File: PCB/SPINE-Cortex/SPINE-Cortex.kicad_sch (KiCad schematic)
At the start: 78 parts, among them J1 SWD, J2 Conn_01x08, J3 Conn_01x02, J4 CAN_IN, J5 CAN_OUT, U1 STM32F103C8Tx, U4 MIC5219-3.3YM5, U5 TCAN1044V, U7 TPS54240DGQ, Y1 Resonator

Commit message: Finish Vertebra
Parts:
- removed C6: 100nF, Capacitor_SMD:C_0603_1608Metric, symbol Device:C_Small
- removed J2: Conn_01x08, Connector_JST:JST_GH_SM08B-GHS-TB_1x08-1MP_P1.25mm_Horizontal, symbol Connector_Generic:Conn_01x08
- removed J3: Conn_01x02, Connector_PinHeader_2.00mm:PinHeader_1x02_P2.00mm_Vertical, symbol Connector_Generic:Conn_01x02
- removed R17: 10K, Resistor_SMD:R_0603_1608Metric, symbol Device:R_Small
- removed U1: STM32F103C8Tx, Package_QFP:LQFP-48_7x7mm_P0.5mm, symbol MCU_ST_STM32F1:STM32F103C8Tx
- added C1: 100nF, Capacitor_SMD:C_0603_1608Metric, symbol Device:C
- added J2: Conn_01x06, Connector_JST:JST_GH_SM06B-GHS-TB_1x06-1MP_P1.25mm_Horizontal, symbol Connector_Generic:Conn_01x06
- added R16: 120R, Resistor_SMD:R_0603_1608Metric, symbol Device:R_Small
- added U1: STM32G431RBTx, Package_QFP:LQFP-64_10x10mm_P0.5mm, symbol MCU_ST_STM32G4:STM32G431RBTx
- added U3: SP3485EN, Package_SO:SOIC-8_3.9x4.9mm_P1.27mm, symbol Interface_UART:SP3485EN
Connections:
- net +3.3V: now also U1.1 (VBAT), U1.16 (VDD), U1.32 (VDD), U1.48 (VDD), U1.64 (VDD)
- net +5V: now also C1.2, J2.2 (Pin_2), U3.8 (VCC)
- net BOOT: now also U1.7 (PG10)
- net CANRX: now also U1.45 (PA11)
- net CANTX: now also U1.46 (PA12)
- net GND: now also C1.1, J2.1 (Pin_1), U1.15 (VSS), U1.27 (VSSA), U1.31 (VSS), U1.47 (VSS), U1.63 (VSS), U3.5 (GND)
- net Reset: now also U1.28 (VREF+)
- net SWCLK: now also U1.50 (PA14)
- net SWDIO: now also U1.49 (PA13)
- net VREF: now also U1.29 (VDDA)
- net at Y1.1: now also U1.5 (PF0)
- net at Y1.3: now also U1.6 (PF1)
- new net ENABLE: J2.6 (Pin_6)
- new net FAULT: J2.5 (Pin_5)
- new net RS485_A: J2.3 (Pin_3), R16.1, U3.6 (A)
- new net RS485_B: J2.4 (Pin_4), R16.2, U3.7 (B)
- new net USART2_DE: U3.2 (~{RE}), U3.3 (DE)
- new net USART2_RX: U3.1 (RO)
- new net USART2_TX: U3.4 (DI)
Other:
- moved on the sheet: C21, C23, C24, C26, C28, C31, C4, FB1, H5, H6, J1, J4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

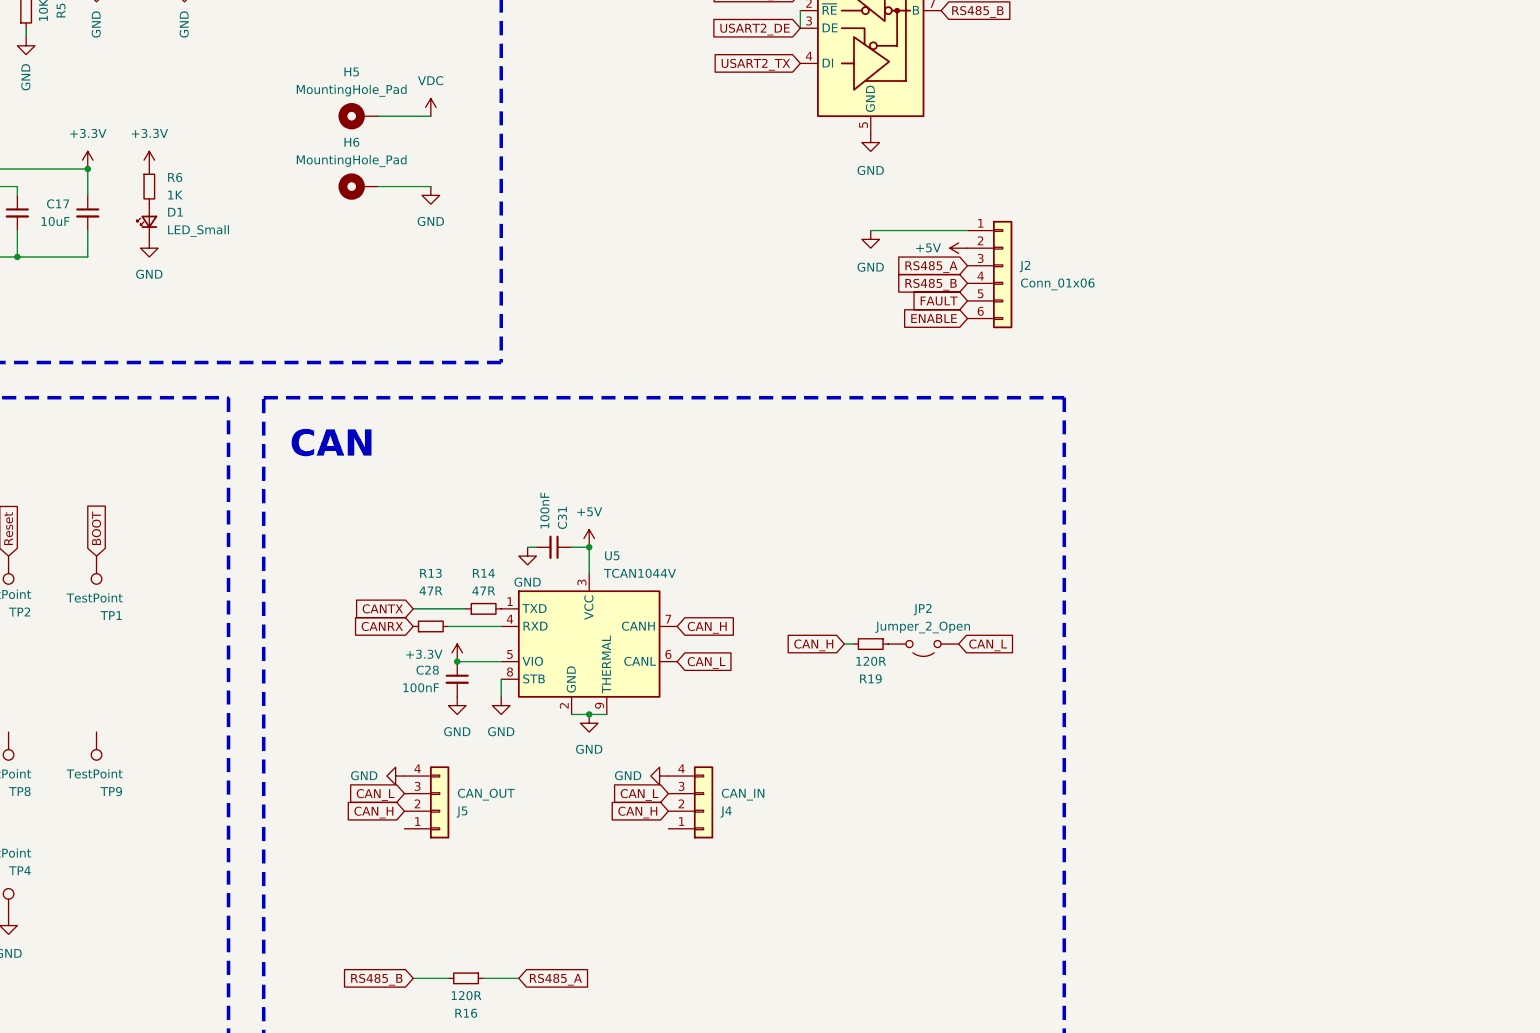
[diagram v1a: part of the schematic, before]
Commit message: Vertebra fix
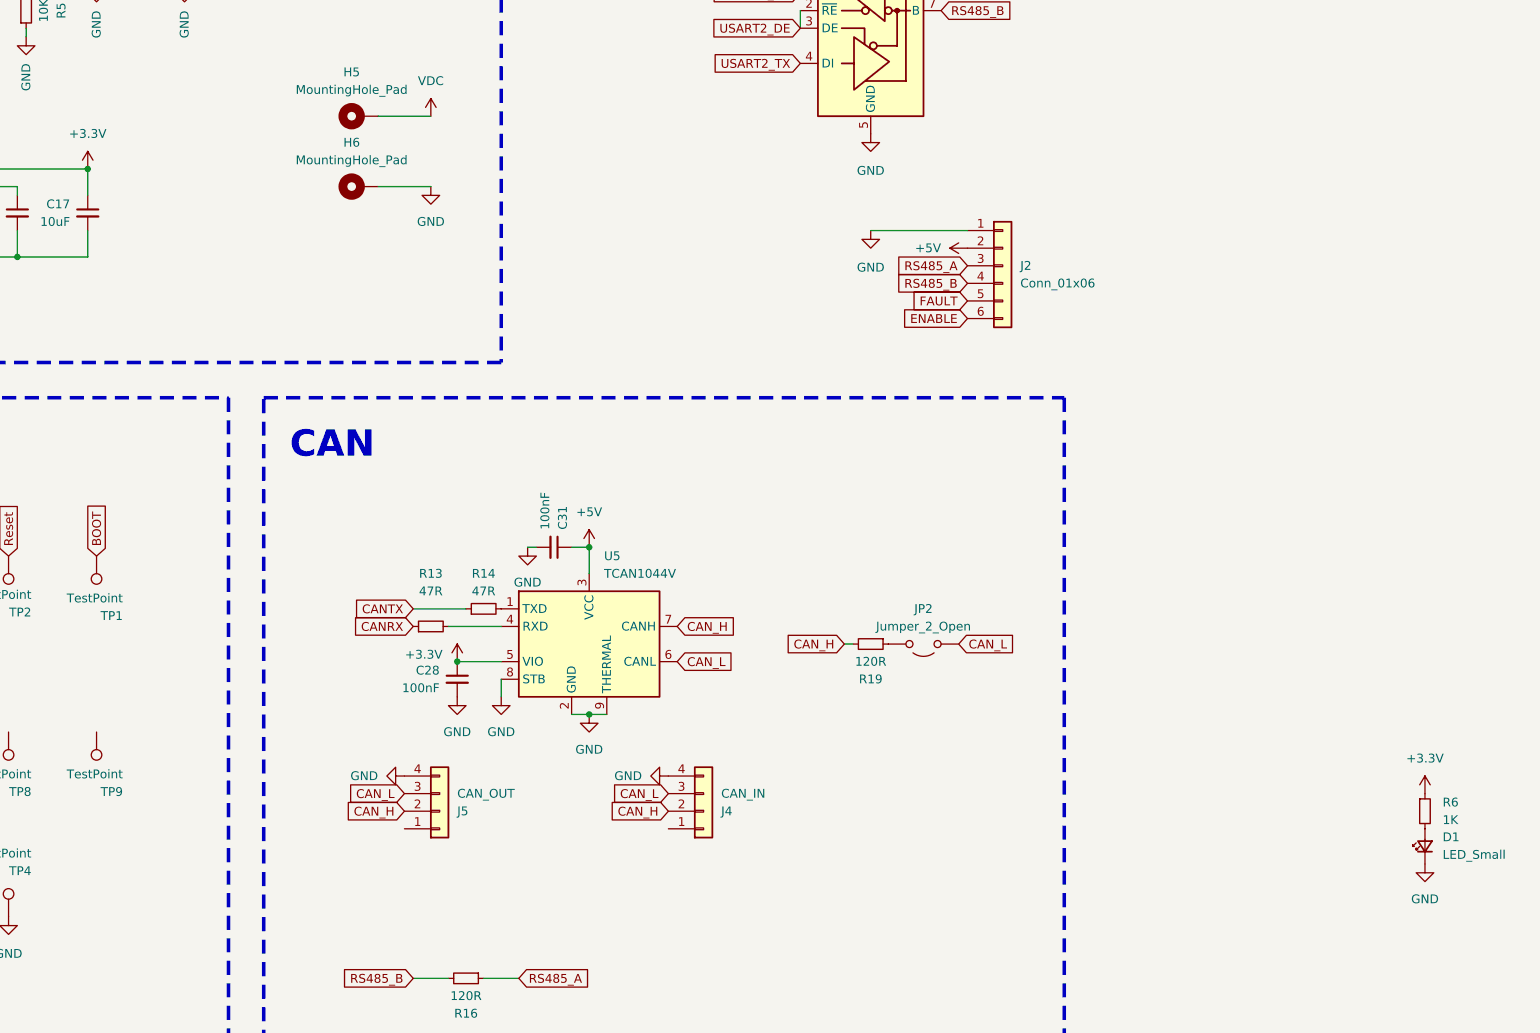
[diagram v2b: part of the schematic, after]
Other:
- moved on the sheet: D1, R6
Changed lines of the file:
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@@
 	(symbol
 		(lib_id "power:+3.3V")
-		(at 162.56 104.14 0)
+		(at 346.71 194.31 0)
 		(unit 1)
 		(exclude_from_sim no)
@@
 		(fields_autoplaced yes)
 		(property "Reference" "#PWR023"
-			(at 162.56 107.95 0)
+			(at 346.71 198.12 0)
 			(effects
 				(font
@@
 		)
 		(property "Value" "+3.3V"
-			(at 162.56 99.06 0)
+			(at 346.71 189.23 0)
 			(effects
 				(font
@@
 		)
 		(property "Footprint" ""
-			(at 162.56 104.14 0)
+			(at 346.71 194.31 0)
 			(effects
 				(font
@@
 		)
 		(property "Datasheet" ""
-			(at 162.56 104.14 0)
+			(at 346.71 194.31 0)
 			(effects
 				(font
@@
 		)
 		(property "Description" "Power symbol creates a global label with name \"+3.3V\""
-			(at 162.56 104.14 0)
+			(at 346.71 194.31 0)
 			(effects
 				(font
@@
 	(symbol
 		(lib_id "Device:R_Small")
-		(at 162.56 106.68 0)
+		(at 346.71 196.85 0)
 		(unit 1)
 		(exclude_from_sim no)
@@
 		(fields_autoplaced yes)
 		(property "Reference" "R6"
-			(at 165.1 105.4099 0)
+			(at 349.25 195.5799 0)
 			(effects
 				(font
@@
 		)
 		(property "Value" "1K"
-			(at 165.1 107.9499 0)
+			(at 349.25 198.1199 0)
 			(effects
 				(font
@@
 		)
 		(property "Footprint" "Resistor_SMD:R_0603_1608Metric"
-			(at 162.56 106.68 0)
+			(at 346.71 196.85 0)
 			(effects
 				(font
@@
 		)
 		(property "Datasheet" "~"
-			(at 162.56 106.68 0)
+			(at 346.71 196.85 0)
 			(effects
 				(font
@@
 		)
 		(property "Description" "Resistor, small symbol"
-			(at 162.56 106.68 0)
+			(at 346.71 196.85 0)
 			(effects
 				(font
@@
 	(symbol
 		(lib_id "Device:LED_Small")
-		(at 162.56 111.76 90)
+		(at 346.71 201.93 90)
 		(unit 1)
 		(exclude_from_sim no)
@@
 		(fields_autoplaced yes)
 		(property "Reference" "D1"
-			(at 165.1 110.4264 90)
+			(at 349.25 200.5964 90)
 			(effects
 				(font
@@
 		)
 		(property "Value" "LED_Small"
-			(at 165.1 112.9664 90)
+			(at 349.25 203.1364 90)
 			(effects
 				(font
@@
 		)
 		(property "Footprint" "LED_SMD:LED_0603_1608Metric"
-			(at 162.56 111.76 90)
+			(at 346.71 201.93 90)
 			(effects
 				(font
@@
 		)
 		(property "Datasheet" "~"
-			(at 162.56 111.76 90)
+			(at 346.71 201.93 90)
 			(effects
 				(font
@@
 		)
 		(property "Description" "Light emitting diode, small symbol"
-			(at 162.56 111.76 0)
+			(at 346.71 201.93 0)
 			(effects
 				(font
@@
 		)
 		(property "Sim.Pin" "1=K 2=A"
-			(at 162.56 111.76 0)
+			(at 346.71 201.93 0)
 			(effects
 				(font
@@
 	(symbol
 		(lib_id "power:GND")
-		(at 162.56 114.3 0)
+		(at 346.71 204.47 0)
 		(unit 1)
 		(exclude_from_sim no)
@@
 		(fields_autoplaced yes)
 		(property "Reference" "#PWR070"
-			(at 162.56 120.65 0)
+			(at 346.71 210.82 0)
 			(effects
 				(font
@@
 		)
 		(property "Value" "GND"
-			(at 162.56 119.38 0)
+			(at 346.71 209.55 0)
 			(effects
 				(font
@@
 		)
 		(property "Footprint" ""
-			(at 162.56 114.3 0)
+			(at 346.71 204.47 0)
 			(effects
 				(font
@@
 		)
 		(property "Datasheet" ""
-			(at 162.56 114.3 0)
+			(at 346.71 204.47 0)
 			(effects
 				(font
@@
 		)
 		(property "Description" "Power symbol creates a global label with name \"GND\" , ground"
-			(at 162.56 114.3 0)
-			(effects
-				(font
+			(at 346.71 204.47 0)
+			(effects
+				(font

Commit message: update
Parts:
- removed C4: 100nF, Capacitor_SMD:C_0603_1608Metric, symbol Device:C_Small
- removed C45: 10uF, Capacitor_SMD:C_1206_3216Metric, symbol Device:C
- removed TH1: Thermistor_NTC, Resistor_SMD:R_0603_1608Metric, symbol Device:Thermistor_NTC
- removed U1: STM32G431RBTx, Package_QFP:LQFP-64_10x10mm_P0.5mm, symbol MCU_ST_STM32G4:STM32G431RBTx
- added BZ1: Buzzer, Buzzer_Beeper:Buzzer_12x9.5RM7.6, symbol Device:Buzzer
- added C3, C6: 100nF, Capacitor_SMD:C_0603_1608Metric, symbol Device:C_Small
- added D2: B5819WS, Diode_SMD:D_0805_2012Metric, symbol Device:D_Schottky_Small_Filled
- added D3: WS2812B-2020, LED_SMD:LED_WS2812B-2020_PLCC4_2.0x2.0mm, symbol LED:WS2812B-2020
- added J3: Conn_01x02, Connector_PinHeader_2.00mm:PinHeader_1x02_P2.00mm_Vertical, symbol Connector_Generic:Conn_01x02
- added J6: CAN_IN, Connector_JST:JST_GH_SM04B-GHS-TB_1x04-1MP_P1.25mm_Horizontal, symbol Connector_Generic:Conn_01x04
- added J7: Conn_01x02, TerminalBlock_MetzConnect:TerminalBlock_MetzConnect_Type094_RT03502HBLU_1x02_P5.00mm_Horizontal, symbol Connector_Generic:Conn_01x02
- added Q1, Q2, Q3, Q4, Q8: Q_NMOS_GSD, Package_TO_SOT_SMD:SOT-23, symbol Transistor_FET:Q_NMOS_GSD
- added Q7: Q_PMOS_GSD, Package_TO_SOT_SMD:SOT-23, symbol Transistor_FET:Q_PMOS_GSD
- added R17, R18, R20, R22, R26: 10K, Resistor_SMD:R_0603_1608Metric, symbol Device:R_Small
- added R21, R24: 1K, Resistor_SMD:R_0603_1608Metric, symbol Device:R_Small
- added R23: 220R, Resistor_SMD:R_0603_1608Metric, symbol Device:R_Small
- added U1: SFH617A-2X009T, Package_DIP:SMDIP-4_W9.53mm_Clearance8mm, symbol Isolator:SFH617A-2X009T
- added U2: STM32G431RBTx, Package_QFP:LQFP-64_10x10mm_P0.5mm, symbol MCU_ST_STM32G4:STM32G431RBTx
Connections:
- net +3.3V: now also C3.1, R24.2, U1.4, U2.1 (VBAT), U2.16 (VDD), U2.32 (VDD), U2.48 (VDD), U2.64 (VDD)
- net +5V: now also BZ1.1 (+), D2.1 (K), J7.2 (Pin_2), Q7.2 (S), R22.2
- net BOOT: now also U2.61 (PB8)
- net CANRX: now also U2.45 (PA11)
- net CANTX: now also U2.46 (PA12)
- net ENABLE: now also J2.5 (Pin_5), Q7.3 (D); no longer J2.6 (Pin_6)
- net FAULT: now also J2.6 (Pin_6), R24.1; no longer J2.5 (Pin_5)
- net GND: now also C3.2, C6.2, J3.1 (Pin_1), Q1.2 (S), Q8.2 (S), R17.1, R21.1, R23.2, R26.1, U2.15 (VSS), U2.27 (VSSA), U2.31 (VSS), U2.47 (VSS), U2.63 (VSS)
- net LED1: now also U2.34 (PB12)
- net LED2: now also U2.35 (PB13)
- net LED3: now also U2.36 (PB14)
- net NTC_1: now also C6.1, J3.2 (Pin_2)
- net Reset: now also U2.7 (PG10)
- net SWCLK: now also U2.50 (PA14)
- net SWDIO: now also U2.49 (PA13)
- net VDC: now also C2.2, C5.2, D4.1 (K), R2.2, U7.2 (VIN); no longer D4.2 (A), H5.1
- net VREF: now also U2.28 (VREF+), U2.29 (VDDA)
- net at Y1.1: now also U2.5 (PF0)
- net at Y1.3: now also U2.6 (PF1)
- new net: Q8.1 (G), R18.1, R26.2
- new net: Q7.1 (G), Q8.3 (D), R22.1
- new net: Q1.1 (G), R17.2, R20.1
- new net: J7.1 (Pin_1), U1.1
- new net: R23.1, U1.2
- new net: BZ1.2 (-), D2.2 (A), Q1.3 (D)
- new net BUZZER: R20.2
- new net PRI_HI: D4.2 (A), H5.1
- new net TIM_BKIN_1: R21.2, U1.3
- new net USART1_RX: U2.44 (PA10)
- new net USART1_TX: U2.43 (PA9)
- new net VERTEBRA_EN: R18.2
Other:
- moved on the sheet: C21, C23, C24, C26, C7, C9, D1, FB1, J1, R6, Y1

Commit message: update
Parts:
- removed C43, C44: 10uF, Capacitor_SMD:C_1206_3216Metric, symbol Device:C
- removed D6: LED_RBAG, LED_SMD:LED_Cree-PLCC4_2x2mm_CW, symbol Device:LED_RBAG
- removed J1: SWD, Connector_PinHeader_2.54mm:PinHeader_1x03_P2.54mm_Vertical, symbol Connector_Generic:Conn_01x03
- removed Q2, Q3, Q4: Q_NMOS_GSD, Package_TO_SOT_SMD:SOT-23, symbol Transistor_FET:Q_NMOS_GSD
- removed R11, R12, R8: 1K, Resistor_SMD:R_0603_1608Metric, symbol Device:R_Small
- added C4: 100nF, Capacitor_SMD:C_0603_1608Metric, symbol Device:C
- added D5: LED_Small, LED_SMD:LED_0603_1608Metric, symbol Device:LED_Small
- added D7: B5819WS, Diode_SMD:D_0805_2012Metric, symbol Device:D_Schottky_Small_Filled
- added J9: Conn_02x03_Odd_Even, Connector_PinHeader_2.54mm:PinHeader_2x03_P2.54mm_Vertical, symbol Connector_Generic:Conn_02x03_Odd_Even
- added R25: 1K, Resistor_SMD:R_0603_1608Metric, symbol Device:R_Small
- BZ1: footprint Buzzer_Beeper:Buzzer_12x9.5RM7.6 -> Buzzer_Beeper:MagneticBuzzer_CUI_CMT-8504-100-SMT
- J3: footprint Connector_PinHeader_2.00mm:PinHeader_1x02_P2.00mm_Vertical -> Connector_PinHeader_2.54mm:PinHeader_1x02_P2.54mm_Vertical
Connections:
- net TIM_BKIN_1 is gone; now on net TIM_BKIN_2: R21.2, U1.3
- net +3.3V: now also J9.2 (Pin_2); no longer R6.1
- net +5V: now also D3.4 (VDD), R6.1, D7.2 (A); no longer BZ1.1 (+), D2.1 (K)
- net FAULT: now also U2.20 (PA6)
- net GND: now also D3.2 (VSS), C4.1, D5.1 (K), J9.1 (Pin_1)
- net LED1: now also D3.3 (DIN)
- net SWCLK: now also J9.5 (Pin_5)
- net SWDIO: now also J9.3 (Pin_3)
- net USART1_RX: now also J9.6 (Pin_6)
- net USART1_TX: now also J9.4 (Pin_4)
- net USART2_DE: now also U2.13 (PA1)
- net USART2_RX: now also U2.17 (PA3)
- net USART2_TX: now also U2.14 (PA2)
- net VDC: now also C4.2, R25.1
- net TIM_BKIN_2: now reaches U2.59 (PB6)
- new net: D5.2 (A), R25.2
- new net: BZ1.1 (+), D2.1 (K), D7.1 (K)
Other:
- moved on the sheet: BZ1, C21, C23, C24, C26, C3, D2, D3, J6, Q1, Q7, Q8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

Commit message: update
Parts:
- removed C13: 10uF, Capacitor_SMD:C_0603_1608Metric, symbol Device:C_Small
- removed J9: Conn_02x03_Odd_Even, Connector_PinHeader_2.54mm:PinHeader_2x03_P2.54mm_Vertical, symbol Connector_Generic:Conn_02x03_Odd_Even
- added C10: 100nF, Capacitor_SMD:C_0603_1608Metric, symbol Device:C_Small
- added J1: Conn_01x02, Connector_PinHeader_2.54mm:PinHeader_1x02_P2.54mm_Vertical, symbol Connector_Generic:Conn_01x02
- added J8: Conn_01x03, Connector_PinHeader_2.54mm:PinHeader_1x03_P2.54mm_Vertical, symbol Connector_Generic:Conn_01x03
- added R8: 10K, Resistor_SMD:R_0603_1608Metric, symbol Device:R_Small
- added SW1, SW2: SW_Push, Button_Switch_SMD:SW_SPST_B3S-1000, symbol Switch:SW_Push
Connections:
- net +3.3V: now also R8.2
- net GND: now also C10.2, J1.1 (Pin_1), J8.1 (Pin_1), SW1.2, SW2.2
- net SWCLK: now also J8.3 (Pin_3)
- net SWDIO: now also J8.2 (Pin_2)
- new net NTC_2: C10.1, J1.2 (Pin_2), R8.1
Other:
- moved on the sheet: C21, C23, C24, C26, C3, D1, D5, J7, R21, R23, R24, R25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

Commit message: update
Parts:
- removed TP6: TestPoint, TestPoint:TestPoint_Pad_D1.0mm, symbol Connector:TestPoint
- added C12: 100nF, Capacitor_SMD:C_0603_1608Metric, symbol Device:C_Small
- added R11: 147K, Resistor_SMD:R_0603_1608Metric, symbol Device:R_Small
- added R12: 10K, Resistor_SMD:R_0603_1608Metric, symbol Device:R_Small
- D1, D5: value LED_Small -> LED
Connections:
- net +5V: now also J6.2 (Pin_2)
- net CAN_H: now also JP2.1 (A); no longer R19.2
- net CAN_L: now also R19.2; no longer JP2.1 (A)
- net GND: now also J6.1 (Pin_1), TP7.1, C12.2, R12.1
- net LED1: now also J6.3 (Pin_3), U2.62 (PB9); no longer U2.34 (PB12)
- net NTC_1: now also U2.11 (PC3)
- net NTC_2: now also U2.12 (PA0)
- net TIM_BKIN_2: now also U2.41 (PC9); no longer U2.59 (PB6)
- net USART1_RX: now also TP9.1
- net USART1_TX: now also TP8.1
- net VDC: now also R11.2
- net VERTEBRA_EN: now also U2.40 (PC8)
- net at D3.1 (DOUT): now also J6.4 (Pin_4)
- net BUTTON_1: now reaches SW2.1
- net BUTTON_1: now also U2.25 (PB1)
- net V_SENSE: now reaches U2.10 (PC2)
- net V_SENSE: now also C12.1, R11.1, R12.2
- net BUTTON_2: now reaches U2.26 (PB2)
- net BUTTON_2: now also SW1.1
- net LED2: no longer names the net of U2.35 (PB13)
- net LED3: no longer names the net of U2.36 (PB14)
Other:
- note added: "."
- note added: "ENABLE"
- note added: "FAULT"
- note added: "RS485"
- moved on the sheet: BZ1, C1, C10, C19, C6, D1, D2, D3, D5, D7, J1, J2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

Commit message: update
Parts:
- R20: value 10K -> 47R
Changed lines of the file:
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@@
 			)
 		)
-		(property "Value" "10K"
+		(property "Value" "47R"
 			(at 320.04 180.34 90)
 			(effects
